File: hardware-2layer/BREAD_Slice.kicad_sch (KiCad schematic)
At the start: 14 parts, among them J1 Conn_01x10_Female

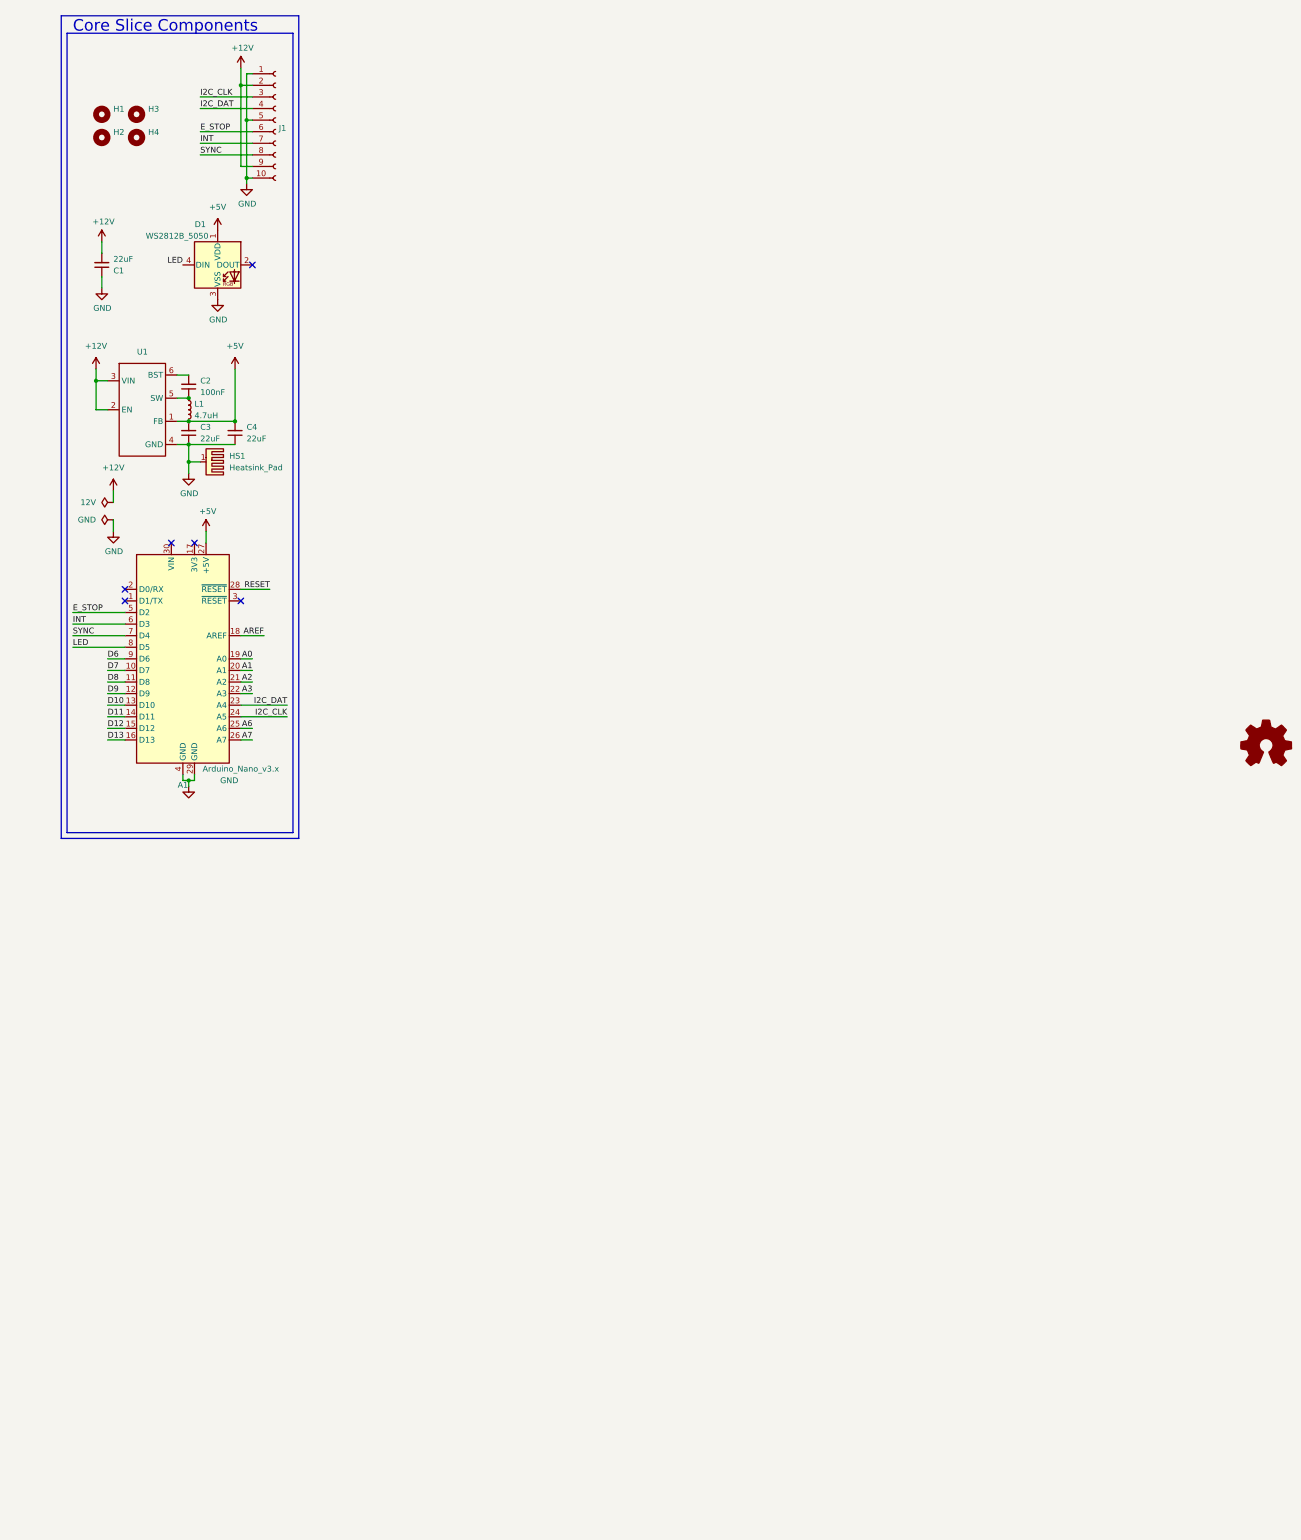
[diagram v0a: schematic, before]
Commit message: added updated 2layer and 4layer tempaltes
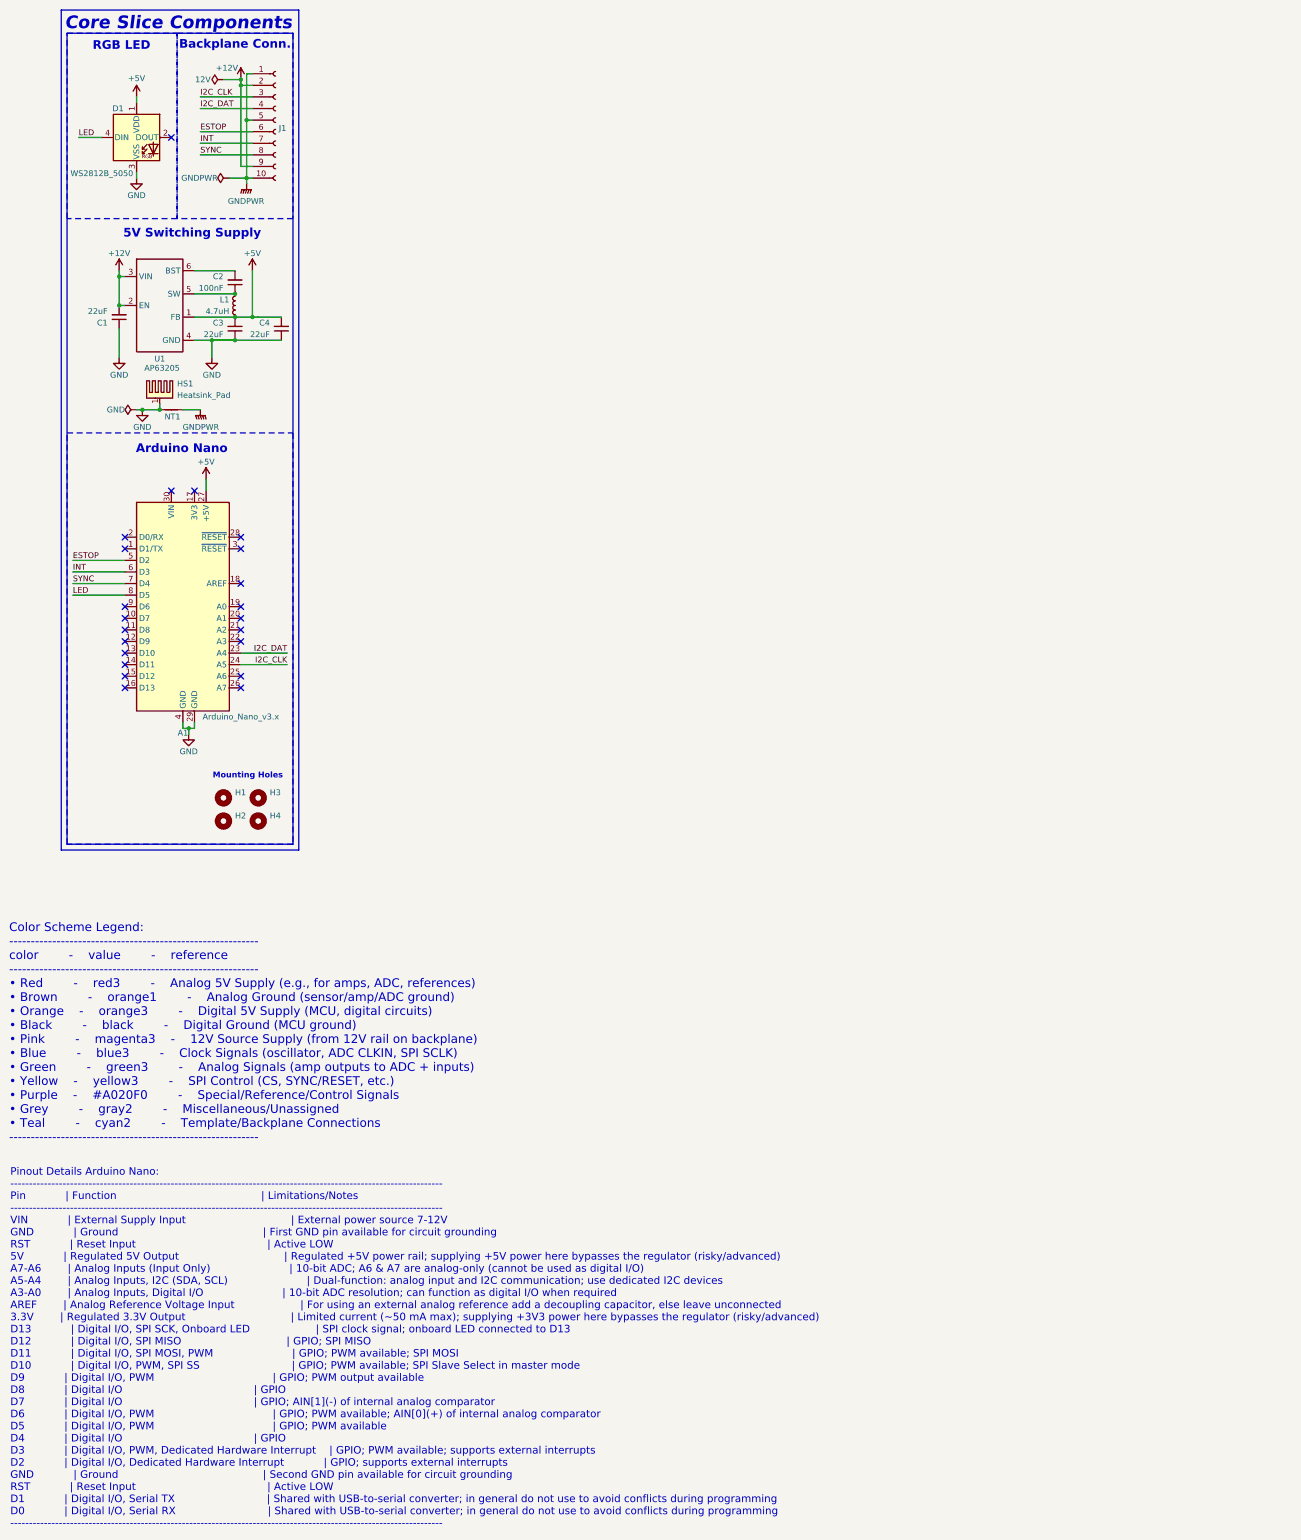
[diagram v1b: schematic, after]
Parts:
- added NT1: NetTie_2, NetTie:NetTie-2_SMD_Pad2.0mm, symbol Device:NetTie_2
- D1: PROD_ID (none) -> DIO-12503
- HS1: footprint KML-Custom:Thermal Pad -> kml-custom:Thermal Pad
- U1: value ~ -> AP63205
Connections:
- net GND: now also NT1.1; no longer J1.1 (Pin_1), J1.10 (Pin_10), J1.5 (Pin_5)
- net A0: no longer names the net of A1.19 (A0)
- net A1: no longer names the net of A1.20 (A1)
- net A2: no longer names the net of A1.21 (A2)
- net A3: no longer names the net of A1.22 (A3)
- net A6: no longer names the net of A1.25 (A6)
- net A7: no longer names the net of A1.26 (A7)
- net AREF: no longer names the net of A1.18 (AREF)
- net D10: no longer names the net of A1.13 (D10)
- net D11: no longer names the net of A1.14 (D11)
- net D12: no longer names the net of A1.15 (D12)
- net D13: no longer names the net of A1.16 (D13)
- net D6: no longer names the net of A1.9 (D6)
- net D7: no longer names the net of A1.10 (D7)
- net D8: no longer names the net of A1.11 (D8)
- net D9: no longer names the net of A1.12 (D9)
- net E_STOP renamed ESTOP
- net RESET: no longer names the net of A1.28 (~{RESET})
- new net GNDPWR: J1.1 (Pin_1), J1.10 (Pin_10), J1.5 (Pin_5), NT1.2
- no-connect marks 6 -> 22
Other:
- note added: "5V Switching Supply"
- note added: "Arduino Nano"
- note added: "Backplane Conn."
- note added: "Color Scheme Legend: ---------------------------------------------------------- color - value - reference ---------------------------------------------------------- • Red - red3 - Analog 5V Supply (e.g., for amps, ADC, references) • Brown - orange1 - Analog Ground (sensor/amp/ADC ground) • Orange - orange3 - Digital 5V Supply (MCU, digital circuits) • Black - black - Digital Ground (MCU ground) •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"
- note added: "Mounting Holes"
- note added: "Pinout Details Arduino Nano: -------------------------------------------------------------------------------------------------------------------- Pin | Function | Limitations/Notes -------------------------------------------------------------------------------------------------------------------- VIN | External Supply Input | External power source 7-12V GND | Ground | First GND pin available for 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"
- note added: "RGB LED"
- moved on the sheet: A1, C1, C2, C3, C4, H1, H2, H3, H4, L1, U1
